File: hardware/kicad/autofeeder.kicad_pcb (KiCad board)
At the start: 2 copper layers, 56 x 54 mm, 0 parts

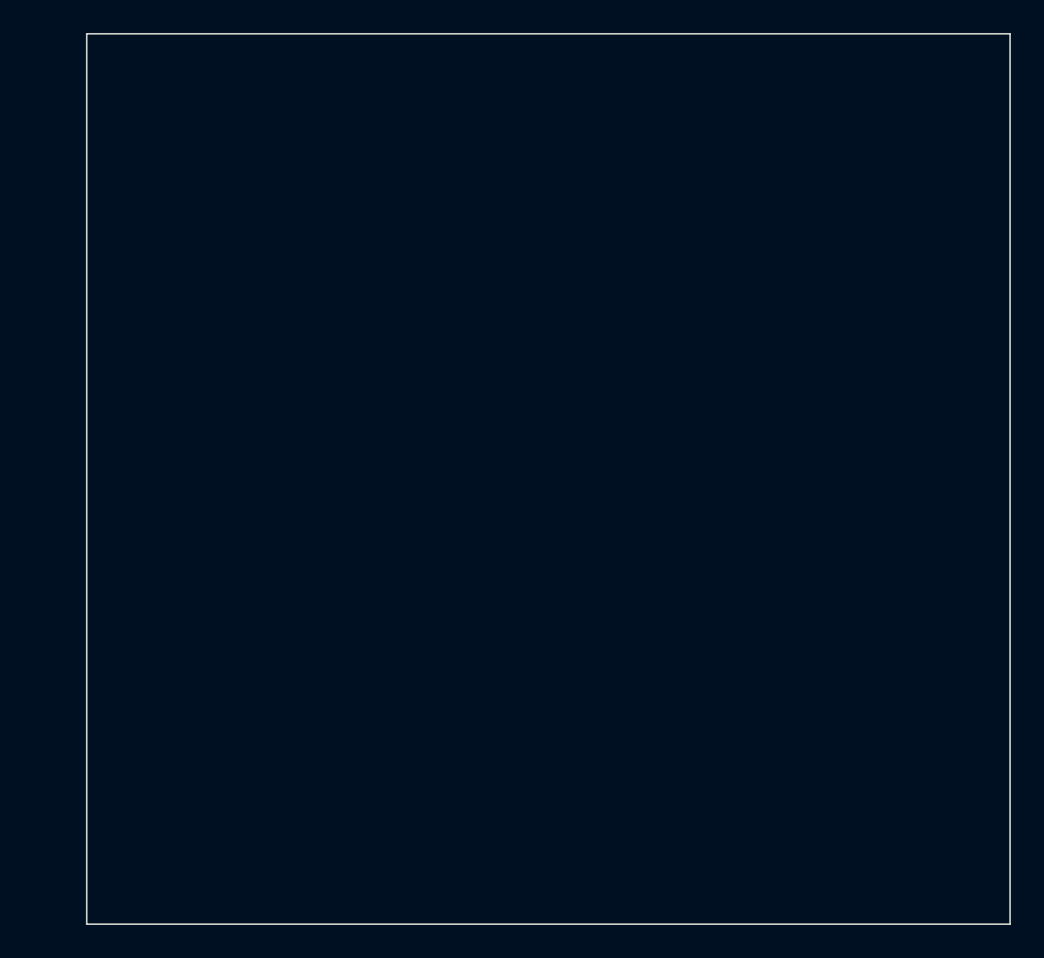
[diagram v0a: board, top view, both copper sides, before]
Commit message: Snapshot current design (ESP32-C6-Zero, RT6150A buck-boost, FS8205A protection)
- Switch from ESP32-C6-WROOM module to Waveshare ESP32-C6-Zero (socketed)
- Replace TPS63802 (QFN) with RT6150A (SOT-23-6, hand-solderable)
- Split DW01A+FS8205A into separate U3/U8 symbols (SOT-23-6)
- Add gerber/drill/CPL fabrication output
- Add mounting holes and OLED SPI display footprint
- Generate schematic + PCB from Python pipeline scripts
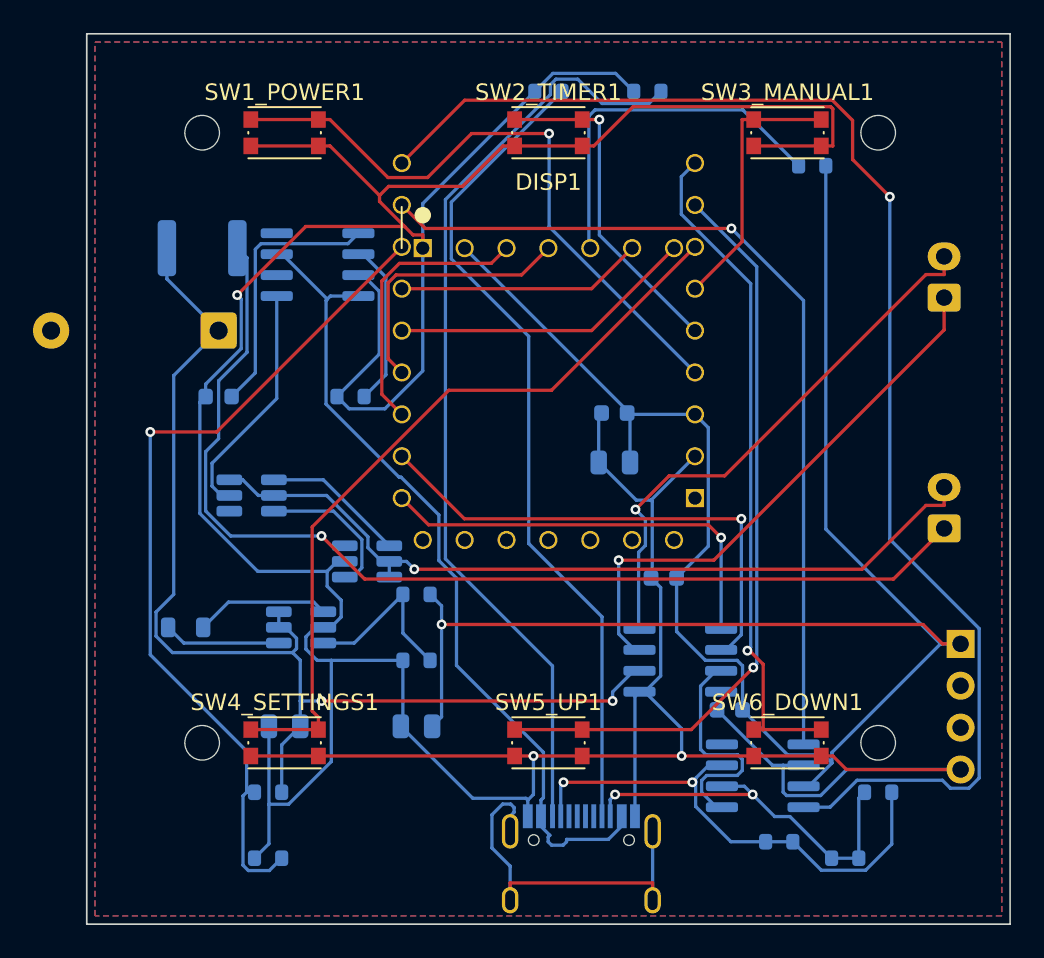
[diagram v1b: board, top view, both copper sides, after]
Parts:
- added C1: C_0603_1608Metric, C_0603_1608Metric, B.Cu at (32.0, 23.0)
- added C2: C_0805_2012Metric, C_0805_2012Metric, B.Cu at (32.0, 26.0)
- added C3: C_0603_1608Metric, C_0603_1608Metric, B.Cu at (35.0, 33.0)
- added C4: C_0805_2012Metric, C_0805_2012Metric, B.Cu at (12.0, 42.0)
- added C5: C_0805_2012Metric, C_0805_2012Metric, B.Cu at (20.0, 42.0)
- added C6: C_0603_1608Metric, C_0603_1608Metric, B.Cu at (39.0, 41.0)
- added D1: D_DO-41_SOD81_P10.16mm_Horizontal, D_DO-41_SOD81_P10.16mm_Horizontal, B.Cu at (8.00, 18.0)
- added DISP1: OLED_1.3in_SSD1306_SPI, OLED_1.3in_SSD1306_SPI, F.Cu at (28.0, 24.0)
- added F1: Fuse_1812_4532Metric, Fuse_1812_4532Metric, B.Cu at (7.00, 13.0)
- added H1: MountingHole_2.1mm_NPTH, MountingHole_2.1mm_NPTH, F.Cu at (7.00, 6.00)
- added H2: MountingHole_2.1mm_NPTH, MountingHole_2.1mm_NPTH, F.Cu at (7.00, 43.0)
- added H3: MountingHole_2.1mm_NPTH, MountingHole_2.1mm_NPTH, F.Cu at (48.0, 6.00)
- added H4: MountingHole_2.1mm_NPTH, MountingHole_2.1mm_NPTH, F.Cu at (48.0, 43.0)
- added J1: JST_XH_B2B-XH-A_1x02_P2.50mm_Vertical, JST_XH_B2B-XH-A_1x02_P2.50mm_Vertical, B.Cu at (52.0, 30.0)
- added J2: JST_XH_B2B-XH-A_1x02_P2.50mm_Vertical, JST_XH_B2B-XH-A_1x02_P2.50mm_Vertical, B.Cu at (52.0, 16.0)
- added J3: USB_C_Receptacle_HRO_TYPE-C-31-M-12, USB_C_Receptacle_HRO_TYPE-C-31-M-12, B.Cu at (30.0, 51.5)
- added J4: PinHeader_1x04_P2.54mm_Vertical, PinHeader_1x04_P2.54mm_Vertical, B.Cu at (53.0, 37.0)
- added L1: L_0805_2012Metric, L_0805_2012Metric, B.Cu at (6.00, 36.0)
- added LED_CHG1: LED_0603_1608Metric, LED_0603_1608Metric, B.Cu at (8.00, 22.0)
- added R10: R_0603_1608Metric, R_0603_1608Metric, B.Cu at (46.0, 50.0)
- added R11: R_0603_1608Metric, R_0603_1608Metric, B.Cu at (20.0, 34.0)
- added R12: R_0603_1608Metric, R_0603_1608Metric, B.Cu at (20.0, 38.0)
- added R13: R_0603_1608Metric, R_0603_1608Metric, B.Cu at (44.0, 8.00)
- added R2_C1: R_0603_1608Metric, R_0603_1608Metric, B.Cu at (16.0, 22.0)
- added R3: R_0603_1608Metric, R_0603_1608Metric, B.Cu at (11.0, 46.0)
- added R4: R_0603_1608Metric, R_0603_1608Metric, B.Cu at (11.0, 50.0)
- added R5: R_0603_1608Metric, R_0603_1608Metric, B.Cu at (48.0, 46.0)
- added R6: R_0603_1608Metric, R_0603_1608Metric, B.Cu at (42.0, 49.0)
- added R_CC1: R_0603_1608Metric, R_0603_1608Metric, B.Cu at (28.0, 3.50)
- added R_CC2: R_0603_1608Metric, R_0603_1608Metric, B.Cu at (34.0, 3.50)
- added SW1_POWER1: SW_Push_1P1T_NO_CK_KMR2, SW_Push_1P1T_NO_CK_KMR2, F.Cu at (12.0, 6.00)
- added SW2_TIMER1: SW_Push_1P1T_NO_CK_KMR2, SW_Push_1P1T_NO_CK_KMR2, F.Cu at (28.0, 6.00)
- added SW3_MANUAL1: SW_Push_1P1T_NO_CK_KMR2, SW_Push_1P1T_NO_CK_KMR2, F.Cu at (42.5, 6.00)
- added SW4_SETTINGS1: SW_Push_1P1T_NO_CK_KMR2, SW_Push_1P1T_NO_CK_KMR2, F.Cu at (12.0, 43.0)
- added SW5_UP1: SW_Push_1P1T_NO_CK_KMR2, SW_Push_1P1T_NO_CK_KMR2, F.Cu at (28.0, 43.0)
- added SW6_DOWN1: SW_Push_1P1T_NO_CK_KMR2, SW_Push_1P1T_NO_CK_KMR2, F.Cu at (42.5, 43.0)
- added U1: ESP32_C6_Zero, ESP32_C6_Zero, B.Cu at (28.0, 18.0)
- added U2: SOIC-8_3.9x4.9mm_P1.27mm, SOIC-8_3.9x4.9mm_P1.27mm, B.Cu at (14.0, 14.0)
- added U3: SOT-23-6_Handsoldering, SOT-23-6_Handsoldering, B.Cu at (10.0, 28.0)
- added U4: SOT-23-6_Handsoldering, SOT-23-6_Handsoldering, B.Cu at (13.0, 36.0)
- added U5: SOIC-8_3.9x4.9mm_P1.27mm, SOIC-8_3.9x4.9mm_P1.27mm, B.Cu at (36.0, 38.0)
- added U6: SOIC-8_3.9x4.9mm_P1.27mm, SOIC-8_3.9x4.9mm_P1.27mm, B.Cu at (41.0, 45.0)
- added U8: SOT-23-6_Handsoldering, SOT-23-6_Handsoldering, B.Cu at (17.0, 32.0)
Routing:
- net GND: track 0.00 -> 278.2 mm, vias 0 -> 3
- net /VCC_3V3: track 0.00 -> 142.7 mm, vias 0 -> 1
- net /CAN_RX: track 0.00 -> 84.3 mm, vias 0 -> 1
- net /BATT_PROT: track 0.00 -> 69.1 mm, vias 0 -> 2
- net /BATT_P: track 0.00 -> 65.0 mm, vias 0 -> 1
- net /CC2: track 0.00 -> 57.5 mm
- net /CAN_TX: track 0.00 -> 53.7 mm, vias 0 -> 1
- net /BAT_MON: track 0.00 -> 52.0 mm, vias 0 -> 1
- net /VBUS: track 0.00 -> 50.7 mm
- net /CC1: track 0.00 -> 50.5 mm
- net /BATT_N: track 0.00 -> 49.6 mm, vias 0 -> 1
- net /BUTTON_SETTINGS: track 0.00 -> 46.8 mm
- net /BUTTON_UP: track 0.00 -> 45.7 mm, vias 0 -> 1
- net /BUTTON_DOWN: track 0.00 -> 41.1 mm, vias 0 -> 1
- net /BUTTON_POWER: track 0.00 -> 38.8 mm, vias 0 -> 1
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- added copper zone on B.Cu, net GND
- added copper zone on F.Cu, net GND
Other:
- board text added: "BATT"
- board text added: "MOTOR"

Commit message: Add RTC, GPS, pogo pin support and standalone firmware
- Fix GPIO19/GPIO20 pin conflicts: move DISP_DC to GP12 (bottom pad),
  BAT_MON to GP6 (bottom pad)
- Add J_RTC header: DS3231 RTC module on I2C (GP13/GP23)
- Add J_GPS header: NEO-6M/8M GPS module on UART (GP7/GP8)
- Enlarge bottom edge pads 19-25 to 1.0mm drill for 0.9mm pogo pins
- Rewrite ESPHome firmware: DS3231 RTC time, GPS, 6-page display menu,
  4 persistent schedule slots, button-driven local control
- Update pinout, BOM, and PCB placement for all new components
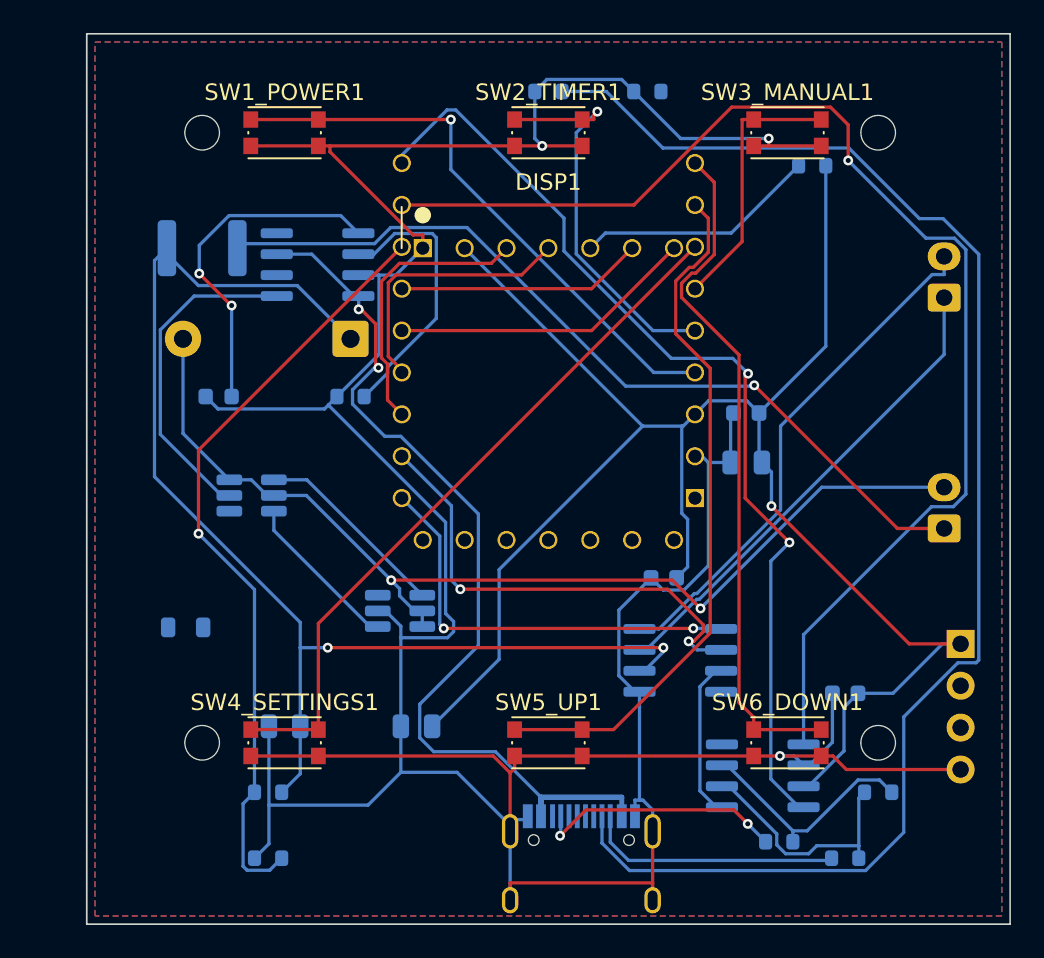
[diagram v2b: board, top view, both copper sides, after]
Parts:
- removed R11, R12: R_0603_1608Metric, R_0603_1608Metric
- removed U4: SOT-23-6_Handsoldering, SOT-23-6_Handsoldering
- moved D1 8.02 mm to (16.0, 18.5)
- moved C1 8.00 mm to (40.0, 23.0)
- moved C2 8.00 mm to (40.0, 26.0)
- moved C6 7.07 mm to (46.0, 40.0)
- moved U8 3.61 mm to (19.0, 35.0)
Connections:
- J3 pad A8: /CAN_H -> /CAN_H_PROT
- J3 pad B8: /CAN_L -> /CAN_L_PROT
- J3 pad S1: unconnected-(J3-SHIELD-PadS1) -> GND
- L1 pad 1: /SW -> /L1_NODE
- L1 pad 2: /VCC_3V3 -> /L2_NODE
- R10 pad 2: /CAN_L -> /CAN_L_PROT
- R6 pad 2: /CAN_H -> /CAN_H_PROT
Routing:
- net /CC2: track 57.5 -> 0.00 mm
- net /CC1: track 50.5 -> 88.5 mm
- net GND: track 278.2 -> 240.3 mm
- net /VCC_3V3: track 142.7 -> 108.6 mm
- net /CAN_RX: track 84.3 -> 59.3 mm, vias 1 -> 2
- net unconnected-(J3-SHIELD-PadS1): track 23.8 -> 0.00 mm
- net /CAN_TX: track 53.7 -> 76.4 mm
- net /CAN_H: track 31.1 -> 14.2 mm, vias 2 -> 0
- net /CAN_L_PROT: track 0.00 -> 15.5 mm
- net /CAN_H_PROT: track 0.00 -> 15.1 mm, vias 0 -> 2
- net /BATT_P: track 65.0 -> 51.0 mm
- net /BATT_N: track 49.6 -> 63.2 mm, vias 1 -> 2
- net /VBUS: track 50.7 -> 62.6 mm, vias 0 -> 2
- net /FB: track 10.7 -> 0.00 mm
- net /CAN_L: track 24.0 -> 14.7 mm, vias 2 -> 0
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
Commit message: Add standalone firmware with RTC, GPS, OLED UI, and menu system
- ESPHome firmware (autofeeder.yaml): RTC timekeeping with DS1307, SNTP+GPS
  fallback, SSD1306 display with clock/manual feed/schedules/GPS/Settings menu,
  6 GPIO buttons, DRV8871 motor control, battery monitoring, CAN bus
- GPS time sync: 30s interval checks TinyGPSPlus, sets system time via
  settimeofday, persists to DS1307 via write_time()
- Hardware: J_RTC at (28,36) back side under OLED, J_GPS at (44,14) top-right,
  U4 TPS63031 WSON-10 footprint fix, bottom pads 19-25 enlarged to 1.0mm for
  0.9mm pogo pins
- Fabrication outputs regenerated (Gerbers, BOM, CPL)
- Docs: pinout.md, bom.md updated for new headers and modules
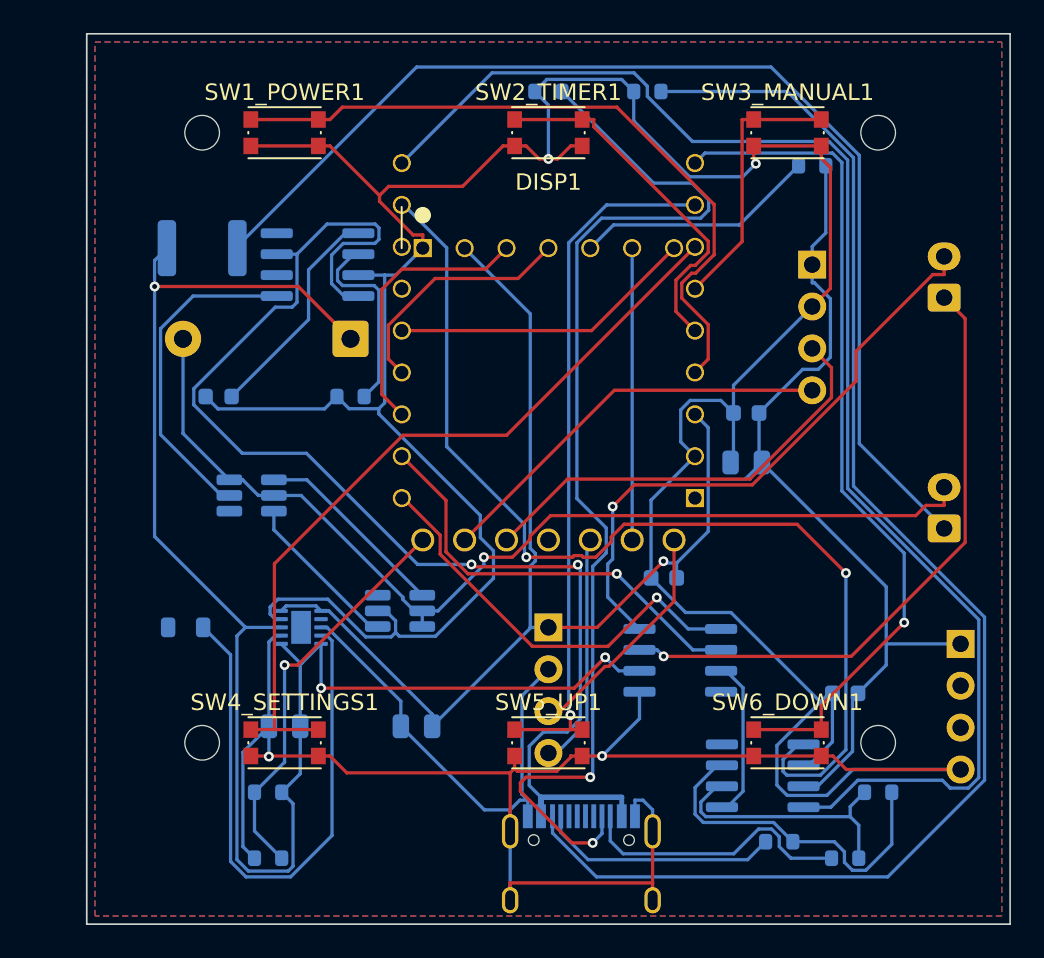
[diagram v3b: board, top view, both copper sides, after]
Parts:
- added J_GPS1: PinHeader_1x04_P2.54mm_Vertical, PinHeader_1x04_P2.54mm_Vertical, B.Cu at (44.0, 14.0)
- added J_RTC1: PinHeader_1x04_P2.54mm_Vertical, PinHeader_1x04_P2.54mm_Vertical, B.Cu at (28.0, 36.0)
- added U4: WSON-10-1EP_2.5x2.5mm_P0.5mm_EP1.2x2mm, WSON-10-1EP_2.5x2.5mm_P0.5mm_EP1.2x2mm, B.Cu at (13.0, 36.0)
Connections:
- U1 pad 15: /DISP_DC -> unconnected-(U1-GP19-Pad15)
- U1 pad 16: /BAT_MON -> unconnected-(U1-GP20-Pad16)
- U1 pad 19: unconnected-(U1-GP13-Pad19) -> /I2C_SDA
- U1 pad 20: unconnected-(U1-GP12-Pad20) -> /DISP_DC
- U1 pad 21: unconnected-(U1-GP23-Pad21) -> /I2C_SCL
- U1 pad 23: unconnected-(U1-GP8/LED-Pad23) -> /GPS_RX
- U1 pad 24: unconnected-(U1-GP7-Pad24) -> /GPS_TX
- U1 pad 25: unconnected-(U1-GP6-Pad25) -> /BAT_MON
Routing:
- net /CC2: track 0.00 -> 85.1 mm
- net GND: track 240.3 -> 308.6 mm, vias 3 -> 4
- net /L1_NODE: track 0.00 -> 35.1 mm
- net /GPS_RX: track 0.00 -> 26.8 mm
- net /CAN_RX: track 59.3 -> 84.4 mm, vias 2 -> 0
- net /GPS_TX: track 0.00 -> 24.8 mm
- net /BATT_PROT: track 75.3 -> 98.6 mm, vias 2 -> 3
- net /VBUS: track 62.6 -> 85.4 mm
- net /BAT_MON: track 47.1 -> 24.7 mm
- net /CC1: track 88.5 -> 67.0 mm, vias 0 -> 2
- net /BATT_P: track 51.0 -> 69.3 mm, vias 1 -> 0
- net /I2C_SCL: track 0.00 -> 14.3 mm
- net /I2C_SDA: track 0.00 -> 14.1 mm
- net /VCC_3V3: track 108.6 -> 122.6 mm
- net /CAN_TX: track 76.4 -> 63.9 mm, vias 1 -> 2
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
